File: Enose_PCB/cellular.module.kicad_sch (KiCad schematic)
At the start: 41 parts, among them J7 U.FL-R-SMT_01_, J8 U.FL-R-SMT_01_, J9 2229333-2, Q1 Q_NPN, Q2 Q_NPN, Q3 Q_NPN, Q4 Q_NPN, Q5 Q_NPN, U4 SIM7070G

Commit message: Updated component values
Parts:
- removed D8: ESD9B3.3ST5G, Diode_SMD:D_SOD-923, symbol Diode:ESD9B3.3ST5G
- removed L4: L_Ferrite, symbol Device:L_Ferrite
- added D?: 0402ESDA-AEC1, 0402ESDA-AEC1:0402ESDAAEC1, symbol Device:D_TVS
- added FB1: MPZ2012S601AT000, Inductor_SMD:L_0805_2012Metric, symbol Device:FerriteBead
- D10: value SP0504BAHT -> ESDALC6V1W5; footprint Package_TO_SOT_SMD:SOT-23-5 -> ESDALC6V1W5:SOT65P210X110-5N
- D11: value ESD9B3.3ST5G -> ESD5Z5.0T1G; footprint Diode_SMD:D_SOD-923 -> Diode_SMD:D_SOD-523
- D12: footprint (none) -> LED_SMD:LED_0201_0603Metric
- D9: footprint (none) -> LED_SMD:LED_0805_2012Metric
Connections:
- net +BATT: now also FB1.2
- net GND: now also D?.1 (A1)
- net RF_ANT: now also D?.2 (A2)
- net at C27.2, C28.2, C29.1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: now also FB1.1
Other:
- moved on the sheet: C32, J7, J8, R26

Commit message: Added LED
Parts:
- R25, R29: value R -> 680
- gave numbers to parts that had none: 1
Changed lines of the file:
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@@
 		(dnp no)
 		(fields_autoplaced yes)
-		(property "Reference" "D?"
+		(property "Reference" "D13"
 			(at 52.07 135.8899 90)
 			(effects
@@
 			(project ""
 				(path "/eef70be0-4107-491c-8ca0-465071a6397e/2117c019-44e0-44cf-b334-dcd1316d0701"
-					(reference "D?")
+					(reference "D13")
 					(unit 1)
 				)
@@
 			)
 		)
-		(property "Value" "R"
+		(property "Value" "680"
 			(at 213.36 134.6199 0)
 			(effects
@@
 			)
 		)
-		(property "Value" "R"
+		(property "Value" "680"
 			(at 265.43 132.0799 0)
 			(effects

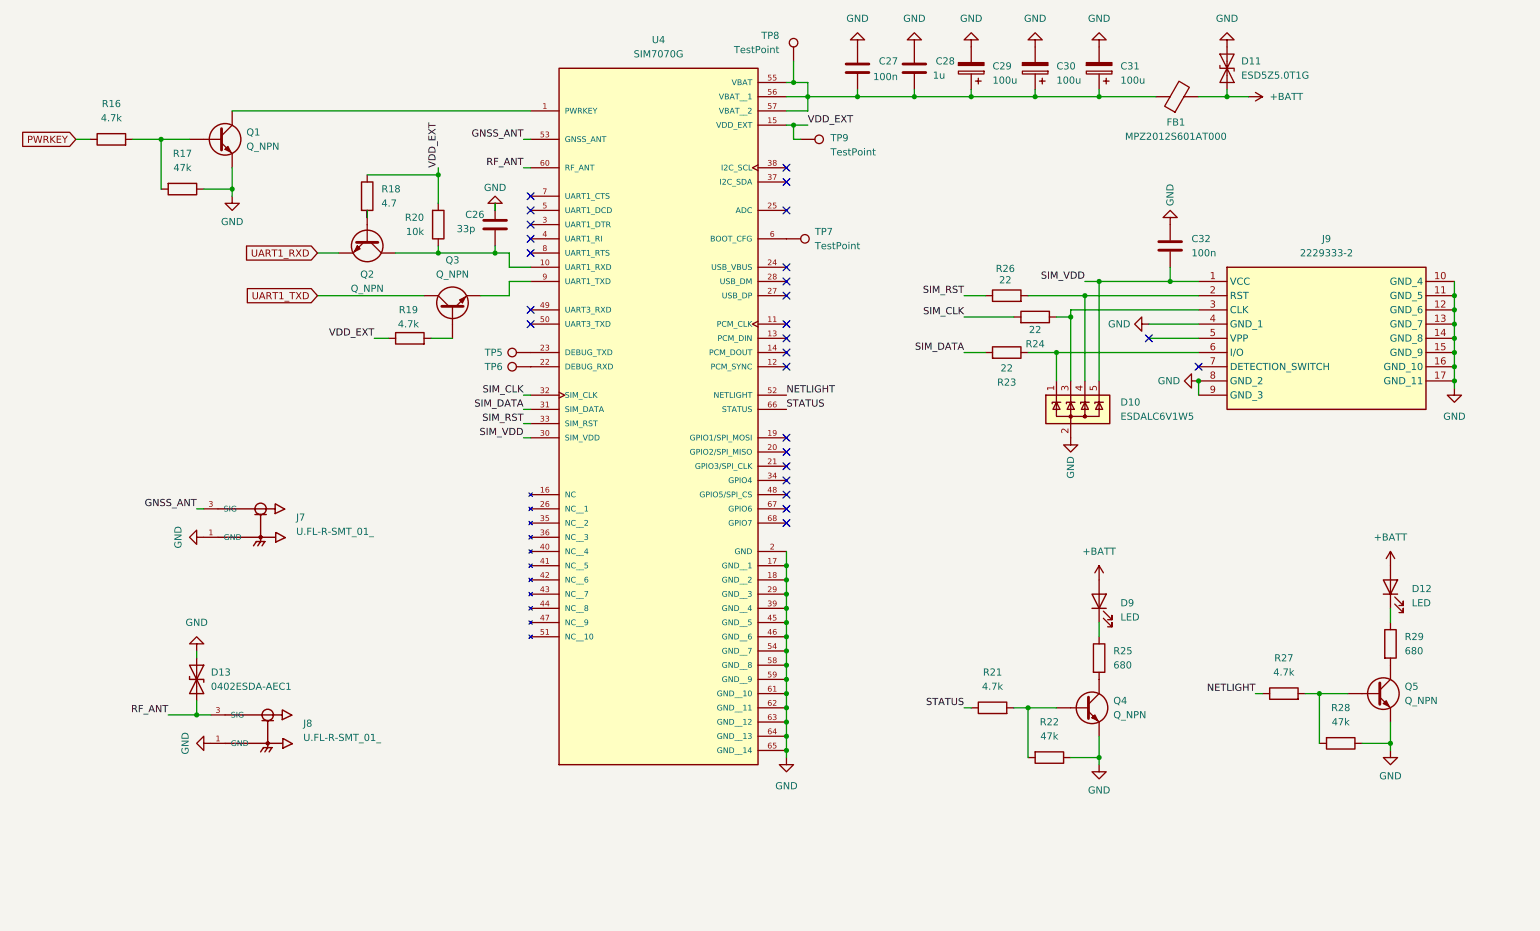
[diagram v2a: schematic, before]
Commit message: Changed Battery Charger
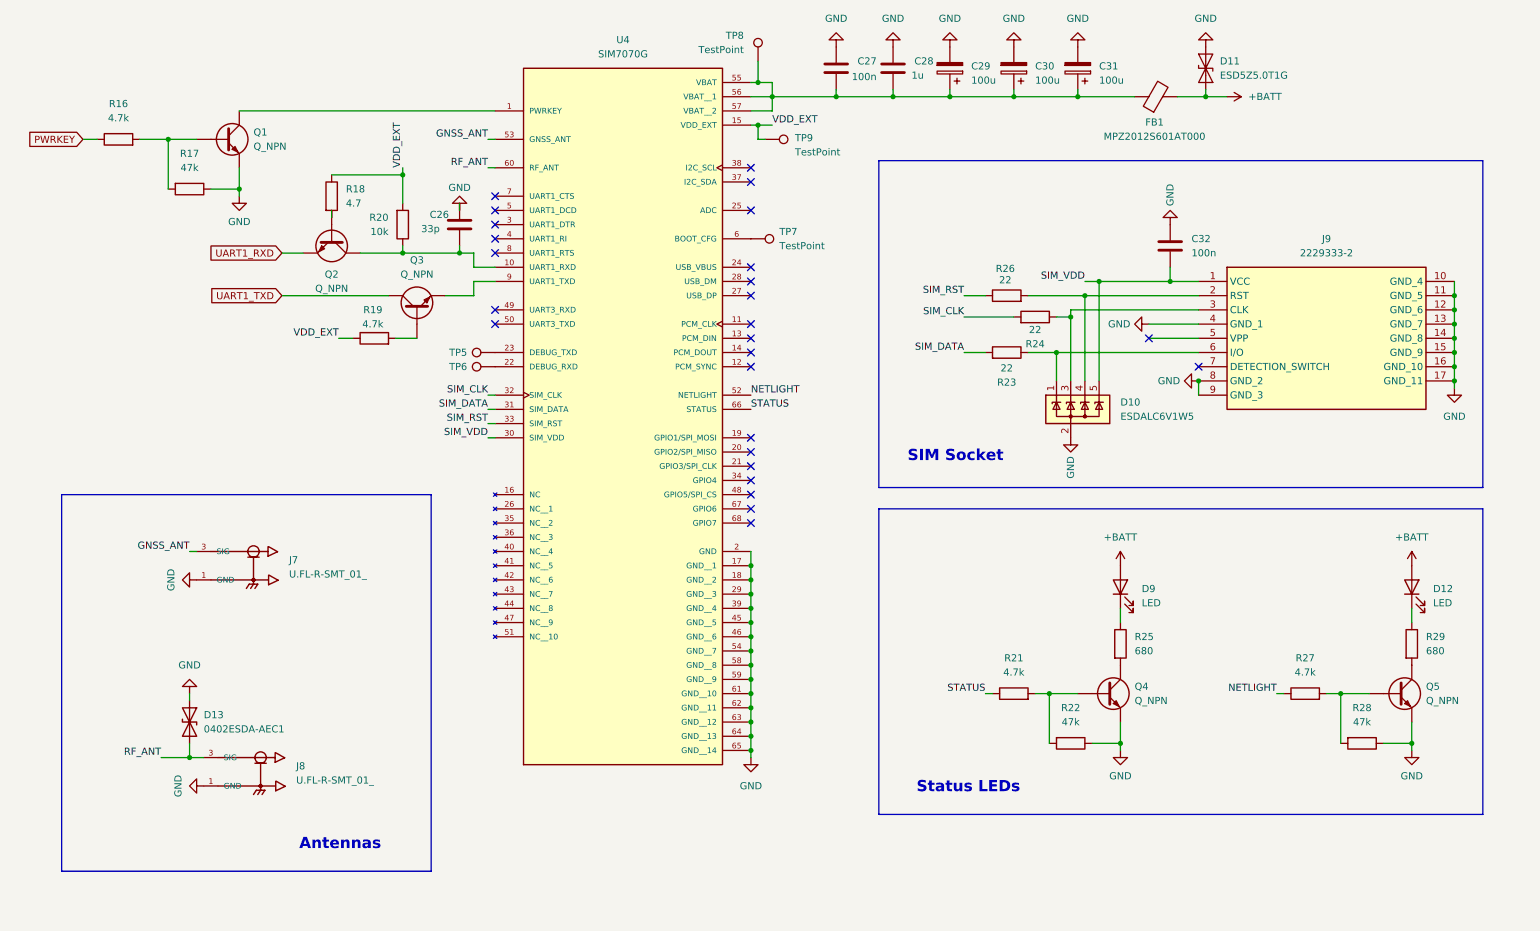
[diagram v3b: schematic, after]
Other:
- note added: "Antennas"
- note added: "SIM Socket"
- note added: "Status LEDs"
- moved on the sheet: C26, C27, C28, C29, C30, C31, D11, D12, D13, D9, FB1, J7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

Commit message: Added load switch and stuff
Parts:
- removed TP7: TestPoint, symbol Connector:TestPoint
- C26, C27, C28, C32: footprint (none) -> Capacitor_SMD:C_0805_2012Metric_Pad1.18x1.45mm_HandSolder
- C29, C30, C31: footprint (none) -> SamacSys_Parts:CAPAE530X610N
- D12: footprint LED_SMD:LED_0201_0603Metric -> LED_SMD:LED_0805_2012Metric_Pad1.15x1.40mm_HandSolder
- D9: footprint LED_SMD:LED_0805_2012Metric -> LED_SMD:LED_0805_2012Metric_Pad1.15x1.40mm_HandSolder
- FB1: footprint Inductor_SMD:L_0805_2012Metric -> Inductor_SMD:L_0805_2012Metric_Pad1.05x1.20mm_HandSolder
- J9: footprint 22293332 -> 2229333-2:22293332
- R16, R17, R18, R19, R20, R21, R22, R23, R24, R25, R26, R27, R28, R29: footprint (none) -> Resistor_SMD:R_0805_2012Metric_Pad1.20x1.40mm_HandSolder
- TP5, TP6, TP8, TP9: footprint (none) -> TestPoint:TestPoint_Pad_1.5x1.5mm
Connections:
- no-connect marks 26 -> 27
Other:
- note added: "Note: - In input decoupling might be exsessive, since we aren't using EDGE or GPRS mode - The module operates with 1.8,V logic levels and therefore requires level shifters for communication with the ESP32 (3.3,V logic) - The selected antenna already has 50ohm impedance, elieminating the need for impedance matching circuitry"
- moved on the sheet: D13, J7, J8

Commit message: Assigned footprints
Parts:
- C26: footprint Capacitor_SMD:C_0805_2012Metric_Pad1.18x1.45mm_HandSolder -> Capacitor_SMD:C_0603_1608Metric_Pad1.08x0.95mm_HandSolder
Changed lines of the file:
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@@
 			)
 		)
-		(property "Footprint" "Capacitor_SMD:C_0805_2012Metric_Pad1.18x1.45mm_HandSolder"
+		(property "Footprint" "Capacitor_SMD:C_0603_1608Metric_Pad1.08x0.95mm_HandSolder"
 			(at 97.4852 59.69 0)
 			(effects
